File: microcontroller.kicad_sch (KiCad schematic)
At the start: 35 parts, among them J1 Micro_SD_Card, J2 TC2030-NL, J3 USB_C_Receptacle, SW1 SW_SPST, SW2 SW_SPST, U1 W25Q128JVS, U2 STM32F411CEUx, U3 USBLC6-2SC6, Y1 8MHz, Y2 32.768KHz

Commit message: Fixed MOSI/MISO on SD
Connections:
- net MISO: now also J1.7 (DAT0/MISO); no longer J1.8 (DAT1/MOSI)
- net MOSI: now also J1.8 (DAT1/MOSI); no longer J1.7 (DAT0/MISO)
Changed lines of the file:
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@@
+	(wire
+		(pts
+			(xy 218.44 100.33) (xy 223.52 100.33)
+		)
+		(stroke
+			(width 0)
+			(type default)
+		)
+	)
+	(wire
+		(pts
+			(xy 151.13 38.1) (xy 157.48 38.1)
+		)
+		(stroke
+			(width 0)
+			(type default)
+		)
+	)
 	(wire
 		(pts
 			(xy 218.44 97.79) (xy 223.52 97.79)
-		)
-		(stroke
-			(width 0)
-			(type default)
-		)
-	)
-	(wire
-		(pts
-			(xy 151.13 38.1) (xy 157.48 38.1)
-		)
-		(stroke
-			(width 0)
-			(type default)
-		)
-	)
-	(wire
-		(pts
-			(xy 218.44 100.33) (xy 223.52 100.33)
 		)
 		(stroke
@@
 	)
 	(label "MOSI"
-		(at 218.44 97.79 0)
+		(at 218.44 100.33 0)
 		(effects
 			(font
@@
 	)
 	(label "MISO"
-		(at 218.44 100.33 0)
-		(effects
-			(font
+		(at 218.44 97.79 0)
+		(effects
+			(font

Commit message: Merges schematics, did annotation
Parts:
- renumbered C12 to C10, C10 to C11, C11 to C12, R8 to R10, R9 to R11, R11 to R4, R10 to R5, R4 to R6, R5 to R7, R6 to R8, R7 to R9

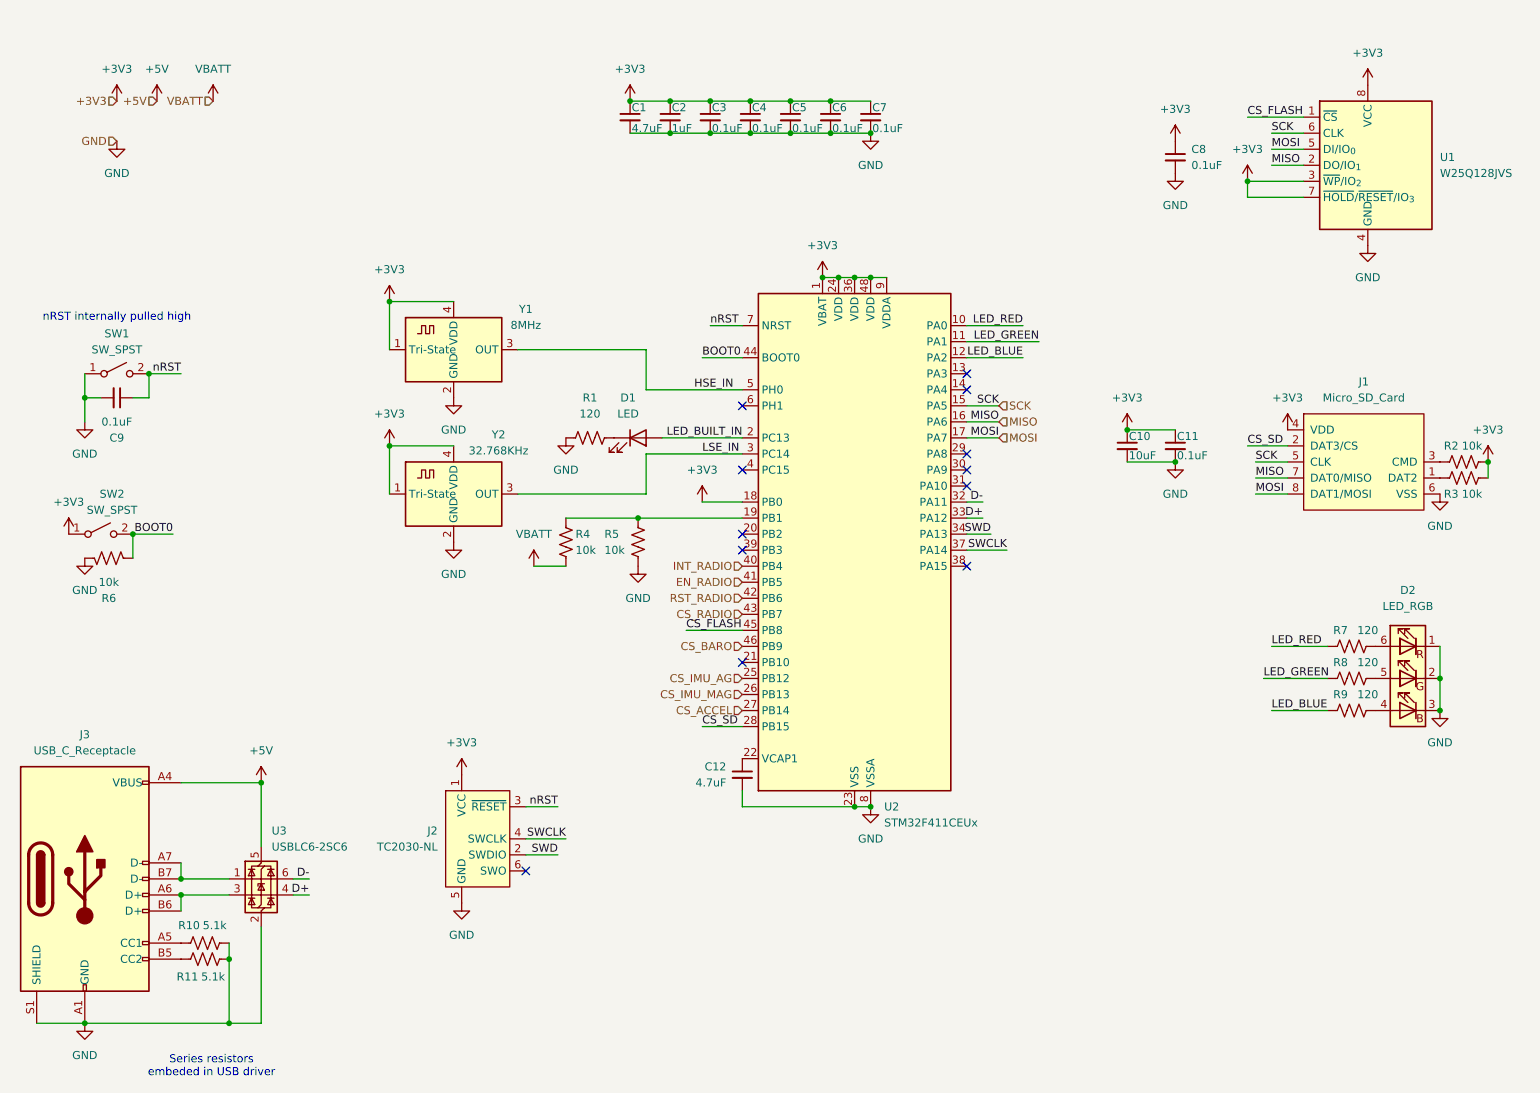
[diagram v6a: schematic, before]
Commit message: Connected topsheet
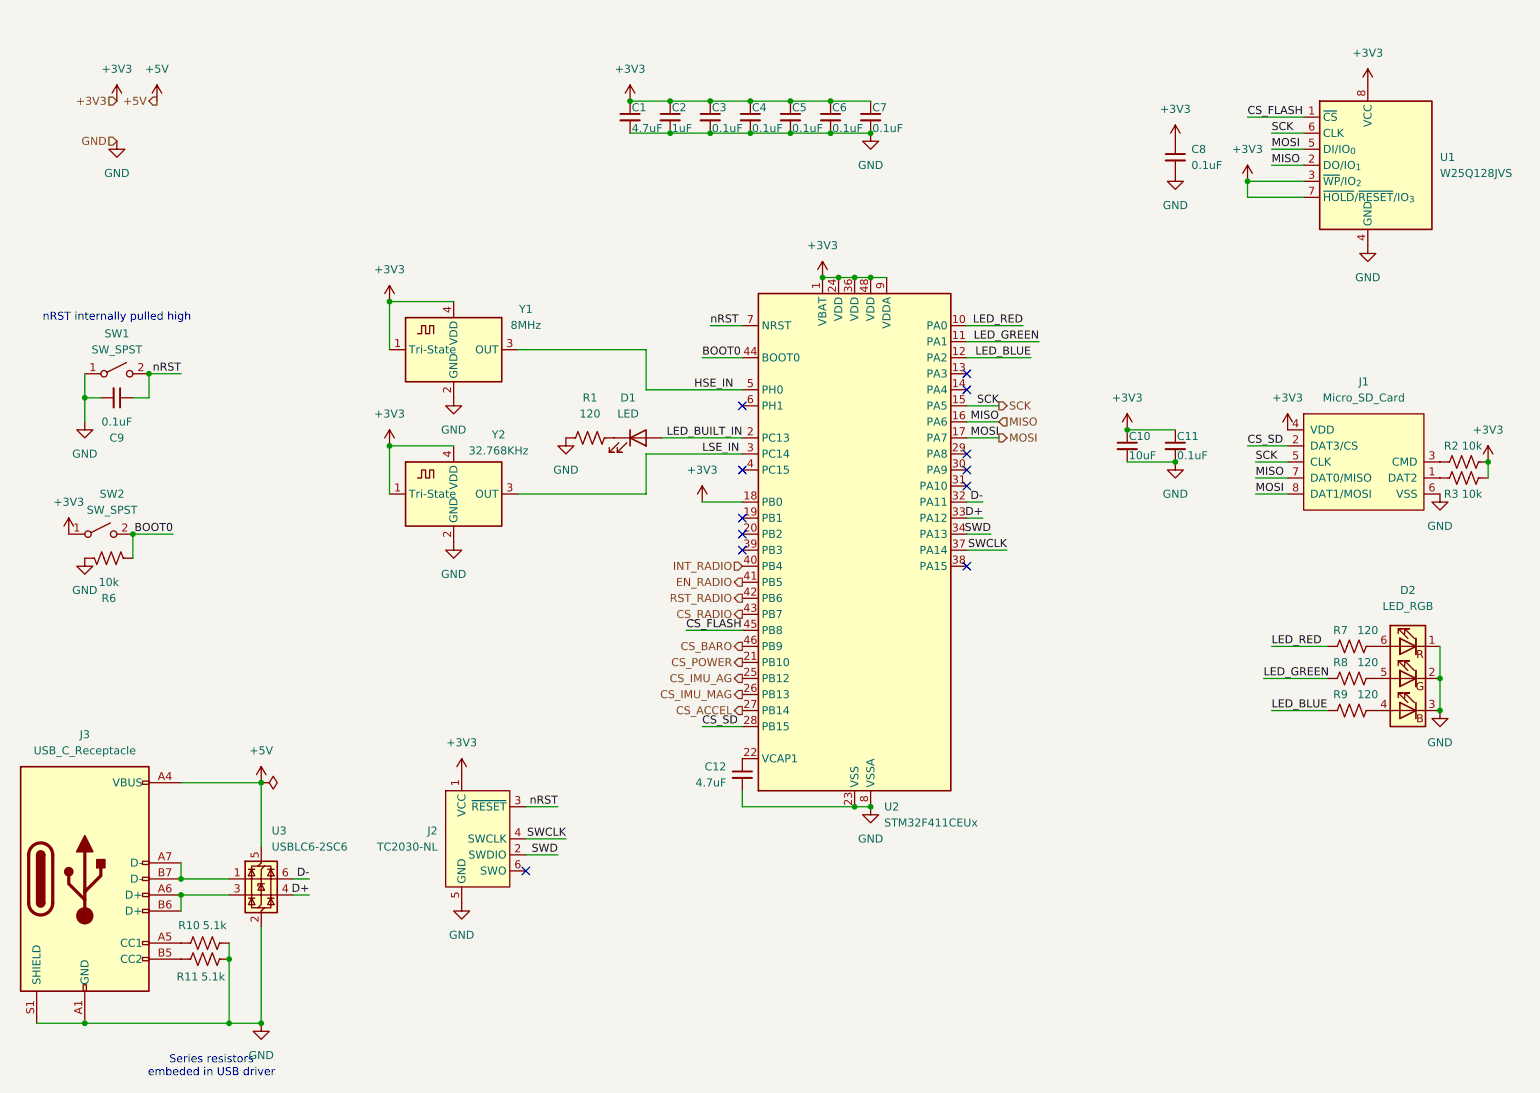
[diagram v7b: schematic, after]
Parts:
- removed R4, R5: 10k, symbol Device:R_US
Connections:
- net CS_POWER: now reaches U2.21 (PB10)

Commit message: Reannotated
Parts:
- renumbered R6 to R4, R7 to R5, R8 to R6, R9 to R7, R10 to R8, R11 to R9
